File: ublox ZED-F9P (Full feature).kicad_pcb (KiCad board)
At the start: 4 copper layers, 43.2 x 43.2 mm, 143 parts, among them J1 Radio, J2 Qwiic Right Angle, J3 PTH, J4 Qwiic Right Angle, J5 USB_C_2-LAYER_PADS, J6 CONN_06NO_SILK_FEMALE_PTH, J7 CONN_09NO_SILK, U2 3.3V, U3 ZED-F9P

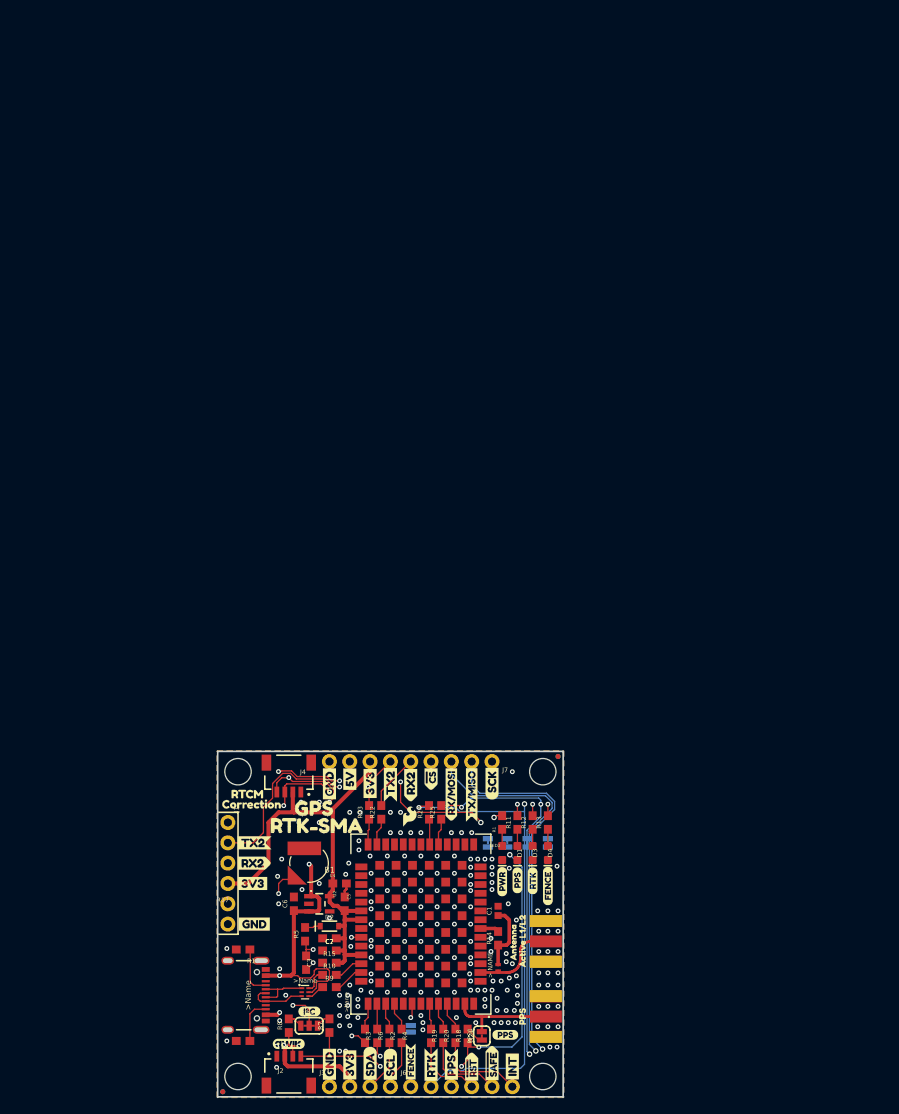
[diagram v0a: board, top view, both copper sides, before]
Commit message: removed SMA time paulse from F9H
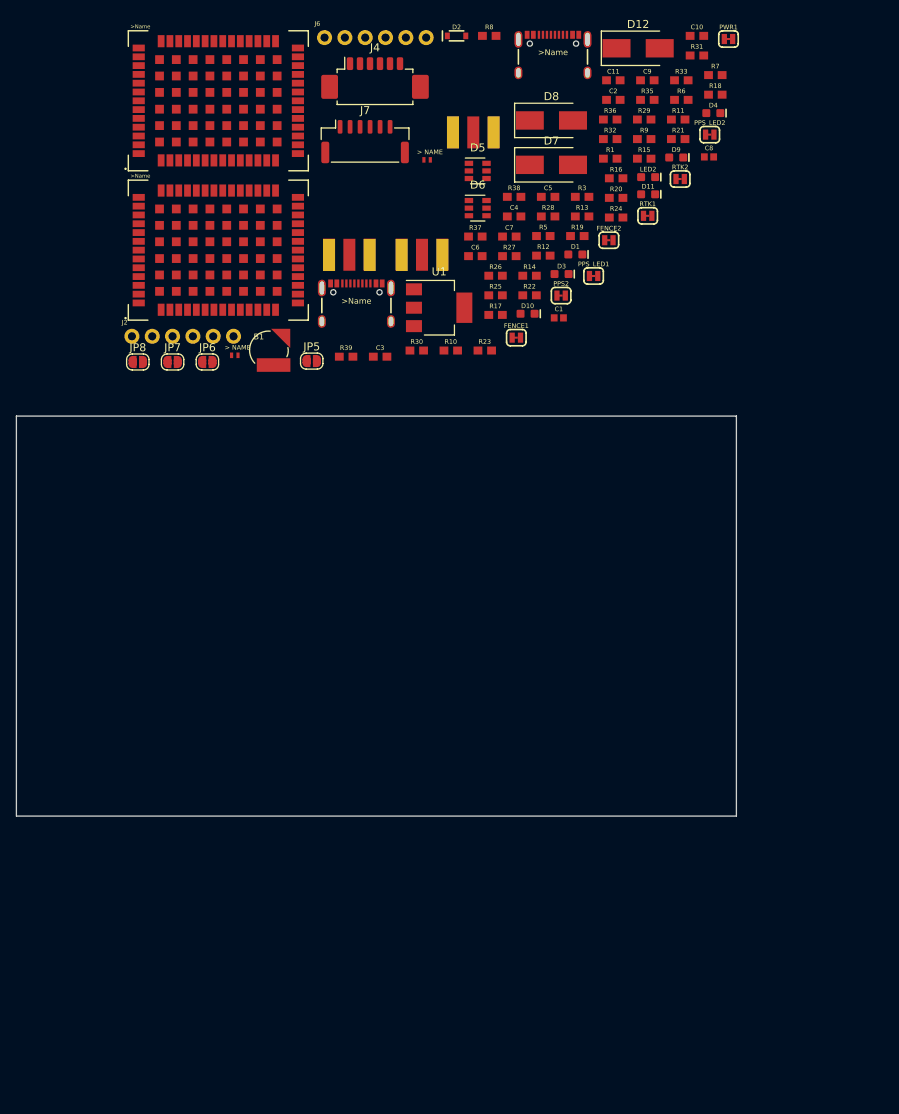
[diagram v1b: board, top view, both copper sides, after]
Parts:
- removed FRAME2: FRAME-LEDGER, Qwiic GPS-RTK-SMA - ublox ZED-F9P:CREATIVE_COMMONS
- removed J3: PTH, Qwiic GPS-RTK-SMA - ublox ZED-F9P:1X04_NO_SILK
- removed JP101, JP31, JP41, JP91: STAND-OFF, Qwiic GPS-RTK-SMA - ublox ZED-F9P:STAND-OFF
- removed JP21, JP61, JP71, JP81: FIDUCIALUFIDUCIAL, Qwiic GPS-RTK-SMA - ublox ZED-F9P:MICRO-FIDUCIAL
- removed LOGO1: OSHW-LOGOMINI, Qwiic GPS-RTK-SMA - ublox ZED-F9P:OSHW-LOGO-MINI
- removed LOGO2: SFE_LOGO_NAME_FLAME.1_INCH, Qwiic GPS-RTK-SMA - ublox ZED-F9P:SFE_LOGO_NAME_FLAME_.1
- removed PPS1: JUMPER-SMT_2_NC_TRACE_SILK, Qwiic GPS-RTK-SMA - ublox ZED-F9P:SMT-JUMPER_2_NC_TRACE_SILK
- removed R2, R4: 33, Qwiic GPS-RTK-SMA - ublox ZED-F9P:0603
- removed SPI1: JUMPER-SMT_2_NO_SILK, Qwiic GPS-RTK-SMA - ublox ZED-F9P:SMT-JUMPER_2_NO_SILK
- removed U$1, U$4: , Qwiic GPS-RTK-SMA - ublox ZED-F9P:SDA-[)
- removed U$10: , Qwiic GPS-RTK-SMA - ublox ZED-F9P:I_SUPER2_C-()-03
- removed U$11, U$54: , Qwiic GPS-RTK-SMA - ublox ZED-F9P:FENCE2
- removed U$12, U$18: , Qwiic GPS-RTK-SMA - ublox ZED-F9P:PWR-()-03
- removed U$13, U$28, U$29, U$32: , Qwiic GPS-RTK-SMA - ublox ZED-F9P:RTK1
- removed U$14, U$17: , Qwiic GPS-RTK-SMA - ublox ZED-F9P:FENCE0
- removed U$15, U$16: , Qwiic GPS-RTK-SMA - ublox ZED-F9P:INT8
- removed U$19, U$20: , Qwiic GPS-RTK-SMA - ublox ZED-F9P:5V
- removed U$2: SPECIAL_INSTRUCTIONS-ORDERING, Qwiic GPS-RTK-SMA - ublox ZED-F9P:ORDERING_INSTRUCTIONS
- removed U$21, U$56, U$58: , Qwiic GPS-RTK-SMA - ublox ZED-F9P:RX20
- removed U$22: , Qwiic GPS-RTK-SMA - ublox ZED-F9P:U#BLOX3
- removed U$23, U$24: , Qwiic GPS-RTK-SMA - ublox ZED-F9P:CS#-_]
- removed U$25, U$52, U$72: , Qwiic GPS-RTK-SMA - ublox ZED-F9P:PPS0
- removed U$26, U$31: , Qwiic GPS-RTK-SMA - ublox ZED-F9P:RX#MOSI3
- removed U$27: , Qwiic GPS-RTK-SMA - ublox ZED-F9P:DSEL0
- removed U$3, U$5: , Qwiic GPS-RTK-SMA - ublox ZED-F9P:SCL-[)
- removed U$30: , Qwiic GPS-RTK-SMA - ublox ZED-F9P:QWIIC_4MM
- removed U$33: , Qwiic GPS-RTK-SMA - ublox ZED-F9P:SFE_LOGO_FLAME_.1
- removed U$34, U$37: , Qwiic GPS-RTK-SMA - ublox ZED-F9P:TX#MISO1
- removed U$35, U$36: , Qwiic GPS-RTK-SMA - ublox ZED-F9P:#RST3
- removed U$38, U$41: , Qwiic GPS-RTK-SMA - ublox ZED-F9P:SCK-(]-04
- removed U$39, U$40: , Qwiic GPS-RTK-SMA - ublox ZED-F9P:#SAFE1
- removed U$42: , Qwiic GPS-RTK-SMA - ublox ZED-F9P:RX22
- removed U$43, U$44: , Qwiic GPS-RTK-SMA - ublox ZED-F9P:PPS5
- removed U$45, U$68: , Qwiic GPS-RTK-SMA - ublox ZED-F9P:GND3
- removed U$47, U$74: , Qwiic GPS-RTK-SMA - ublox ZED-F9P:PPS1
- removed U$48, U$70: , Qwiic GPS-RTK-SMA - ublox ZED-F9P:RTCM5
- removed U$49: , Qwiic GPS-RTK-SMA - ublox ZED-F9P:ZED#F9P6
- removed U$50, U$55, U$57: , Qwiic GPS-RTK-SMA - ublox ZED-F9P:TX21
- removed U$51: , Qwiic GPS-RTK-SMA - ublox ZED-F9P:TX23
- removed U$53, U$69: , Qwiic GPS-RTK-SMA - ublox ZED-F9P:CORRECTION0
- removed U$59: , Qwiic GPS-RTK-SMA - ublox ZED-F9P:GPS0
- removed U$6, U$60, U$61, U$66, U$67, U$7: , Qwiic GPS-RTK-SMA - ublox ZED-F9P:3V3-04
- removed U$62, U$63, U$8, U$9: , Qwiic GPS-RTK-SMA - ublox ZED-F9P:GND-04
- removed U$65: , Qwiic GPS-RTK-SMA - ublox ZED-F9P:ACTIVE_L1#L21
- removed U$71, U$75: , Qwiic GPS-RTK-SMA - ublox ZED-F9P:ANTENNA2
- removed U$73: , Qwiic GPS-RTK-SMA - ublox ZED-F9P:RTK#SMA4
- removed U$76: , Qwiic GPS-RTK-SMA - ublox ZED-F9P:GPS#RTK#SMA5
- removed U2: 3.3V, Qwiic GPS-RTK-SMA - ublox ZED-F9P:SOT23-5
- added C10: 1.0uF, Qwiic GPS-RTK-SMA - ublox ZED-F9P:0603, F.Cu at (186.8, -6.02)
- added C11: 0.1uF, Qwiic GPS-RTK-SMA - ublox ZED-F9P:0603, F.Cu at (176.4, -0.47)
- added C8: 47pF, Qwiic GPS-RTK-SMA - ublox ZED-F9P:0402, F.Cu at (188.3, 9.11)
- added C9: 1.0uF, Qwiic GPS-RTK-SMA - ublox ZED-F9P:0603, F.Cu at (180.6, -0.47)
- added D10: GREEN, Qwiic GPS-RTK-SMA - ublox ZED-F9P:LED-0603, F.Cu at (165.6, 28.7)
- added D11: BLUE, Qwiic GPS-RTK-SMA - ublox ZED-F9P:LED-0603, F.Cu at (180.7, 13.8)
- added D12: DIODE, Diode_SMD:D_SMB_Handsoldering, F.Cu at (179.5, -4.47)
- added D5: USBLC6-2SC6, Package_TO_SOT_SMD:SOT-23-6, F.Cu at (159.4, 10.9)
- added D7: D_Small_ALT, Diode_SMD:D_SMB_Handsoldering, F.Cu at (168.6, 10.1)
- added D8: D_Small_ALT, Diode_SMD:D_SMB_Handsoldering, F.Cu at (168.6, 4.55)
- added D9: Yellow, Qwiic GPS-RTK-SMA - ublox ZED-F9P:LED-0603, F.Cu at (184.2, 9.18)
- added E3: SMA, Qwiic GPS-RTK-SMA - ublox ZED-F9P:SMA-EDGE, F.Cu at (158.9, 6.04)
- added FB2: 120NH, Qwiic GPS-RTK-SMA - ublox ZED-F9P:0402_MURATA, F.Cu at (153.1, 9.47)
- added FENCE2: JUMPER-SMT_2_NC_TRACE_SILK, Qwiic GPS-RTK-SMA - ublox ZED-F9P:SMT-JUMPER_2_NC_TRACE_SILK, F.Cu at (175.8, 19.5)
- added JP6: Jumper_NO_Small, Jumper:SolderJumper-2_P1.3mm_Open_RoundedPad1.0x1.5mm, F.Cu at (125.6, 34.7)
- added JP7: Jumper_NO_Small, Jumper:SolderJumper-2_P1.3mm_Open_RoundedPad1.0x1.5mm, F.Cu at (121.3, 34.7)
- added JP8: Jumper_NO_Small, Jumper:SolderJumper-2_P1.3mm_Open_RoundedPad1.0x1.5mm, F.Cu at (116.9, 34.7)
- added PPS2: JUMPER-SMT_2_NC_TRACE_SILK, Qwiic GPS-RTK-SMA - ublox ZED-F9P:SMT-JUMPER_2_NC_TRACE_SILK, F.Cu at (169.8, 26.4)
- added PPS_LED2: JUMPER-SMT_2_NC_TRACE_SILK, Qwiic GPS-RTK-SMA - ublox ZED-F9P:SMT-JUMPER_2_NC_TRACE_SILK, F.Cu at (188.4, 6.32)
- added R26: 27, Qwiic GPS-RTK-SMA - ublox ZED-F9P:0603, F.Cu at (161.6, 24.0)
- added R27: 100k, Qwiic GPS-RTK-SMA - ublox ZED-F9P:0603, F.Cu at (163.4, 21.5)
- added R28: 33, Qwiic GPS-RTK-SMA - ublox ZED-F9P:0603, F.Cu at (168.2, 16.5)
- added R29: 33, Qwiic GPS-RTK-SMA - ublox ZED-F9P:0603, F.Cu at (180.2, 4.43)
- added R30: 33, Qwiic GPS-RTK-SMA - ublox ZED-F9P:0603, F.Cu at (151.8, 33.3)
- added R31: 33, Qwiic GPS-RTK-SMA - ublox ZED-F9P:0603, F.Cu at (186.8, -3.57)
- added R32: 33, Qwiic GPS-RTK-SMA - ublox ZED-F9P:0603, F.Cu at (176.0, 6.88)
- added R33: 33, Qwiic GPS-RTK-SMA - ublox ZED-F9P:0603, F.Cu at (184.9, -0.47)
- added R35: 1k, Qwiic GPS-RTK-SMA - ublox ZED-F9P:0603, F.Cu at (180.6, 1.98)
- added R36: 1k, Qwiic GPS-RTK-SMA - ublox ZED-F9P:0603, F.Cu at (176.0, 4.43)
- added R37: 1k, Qwiic GPS-RTK-SMA - ublox ZED-F9P:0603, F.Cu at (159.1, 19.1)
- added R38: 33, Qwiic GPS-RTK-SMA - ublox ZED-F9P:0603, F.Cu at (164.0, 14.1)
- added R39: 33, Qwiic GPS-RTK-SMA - ublox ZED-F9P:0603, F.Cu at (143.0, 34.1)
- added RTK2: JUMPER-SMT_2_NC_TRACE_SILK, Qwiic GPS-RTK-SMA - ublox ZED-F9P:SMT-JUMPER_2_NC_TRACE_SILK, F.Cu at (184.7, 11.9)
- added U1: LD1117S33TR, Package_TO_SOT_SMD:SOT-223, F.Cu at (154.6, 28.0)
- added U4: ZED-F9H, Qwiic GPS-RTK-SMA - ublox ZED-F9P:ZED-F9P, F.Cu at (127.0, 2.09)
- C4: value 1.0uF -> 10uF
- D6: value PRTR5V0U2F -> USBLC6-2SC6; footprint Qwiic GPS-RTK-SMA - ublox ZED-F9P:SOT886 -> Package_TO_SOT_SMD:SOT-23-6
- FENCE1, PPS_LED1, PWR1, RTK1: moved to F.Cu
- J1: value Radio -> USB_C_2-LAYER_PADS; footprint Qwiic GPS-RTK-SMA - ublox ZED-F9P:1X06_NO_SILK -> Qwiic GPS-RTK-SMA - ublox ZED-F9P:USB-C-16P-2LAYER-PADS
- J2: value Qwiic Right Angle -> CONN_06NO_SILK_FEMALE_PTH; footprint Qwiic GPS-RTK-SMA - ublox ZED-F9P:JST04_1MM_RA -> Qwiic GPS-RTK-SMA - ublox ZED-F9P:1X06_NO_SILK
- J4: value Qwiic Right Angle -> Molex_PicoBlade; footprint Qwiic GPS-RTK-SMA - ublox ZED-F9P:JST04_1MM_RA -> Connector_Molex:Molex_PicoBlade_53261-0671_1x06-1MP_P1.25mm_Horizontal
- J7: value CONN_09NO_SILK -> JST_GH; footprint Qwiic GPS-RTK-SMA - ublox ZED-F9P:1X09_NO_SILK -> Connector_JST:JST_GH_SM06B-GHS-TB_1x06-1MP_P1.25mm_Horizontal
- JP5: value JUMPER-SMT_3_2-NC_TRACE_SILK -> Jumper_NO_Small; footprint Qwiic GPS-RTK-SMA - ublox ZED-F9P:SMT-JUMPER_3_2-NC_TRACE_SILK -> Jumper:SolderJumper-2_P1.3mm_Open_RoundedPad1.0x1.5mm
- R3, R6: value 33 -> 5.1k
- R7: value 2.2k -> 33
- R8: value 2.2k -> 27
- moved J6 131.6 mm to (140.3, -5.81)
- moved R7 128.2 mm to (189.1, -1.12), turned to 0 degrees
- moved R8 126.2 mm to (160.9, -6.02), turned to 0 degrees
- moved J5 125.5 mm to (168.8, -6.50), turned to 0 degrees
- moved R6 123.0 mm to (184.9, 1.98), turned to 0 degrees
- moved R18 122.1 mm to (189.1, 1.33), turned to 0 degrees
- moved R16 117.5 mm to (176.7, 11.8)
- moved R21 115.1 mm to (184.5, 6.88), turned to 0 degrees
- moved R9 113.1 mm to (180.2, 6.88)
- moved D2 112.4 mm to (156.8, -6.02)
- moved C2 110.7 mm to (176.4, 1.98), turned to 0 degrees
- moved R3 108.3 mm to (172.5, 14.1), turned to 0 degrees
- moved R15 107.9 mm to (180.2, 9.33)
- moved R20 107.0 mm to (176.7, 14.2), turned to 0 degrees
- moved PWR1 104.9 mm to (190.8, -5.63), turned to 0 degrees
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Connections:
- net /D+ renamed /D+_P
- net /D- renamed /D-_P
- net /FENCE_STAT renamed /FENCE_STAT_P
- net /PPS_STAT renamed /PPS_STAT_P
- net /RTK_STAT renamed /RTK_STAT_P
- net /~RESET renamed /~RESET_P
- net /~SAFE renamed /~SAFE_P
- C4 pad 1: 3.3V -> GND
- C4 pad 2: GND -> 3.3V
- C5 pad 2: 3.3V -> Net-(C5-Pad2)
- J2 pad 1: GND -> /FENCE_STAT_H
- J2 pad 2: 3.3V -> /RTK_STAT_H
- J2 pad 3: /SDA/~CS -> /PPS_STAT_H
- J2 pad 4: /SCL/SCK -> /~RESET_H
- J4 pad 1: GND -> /Vcc
- J4 pad 2: 3.3V -> /RX_P
- J4 pad 3: /SDA/~CS -> /TX_P
- J4 pad 4: /SCL/SCK -> /RX_H
- J6 pad 6: /INT -> /INT_P
- J7 pad 1: /SCL/SCK -> /Vcc
- J7 pad 2: /TXO/MISO -> Net-(J7-Pad2)
- J7 pad 3: /RXI/MOSI -> Net-(J7-Pad3)
- J7 pad 4: /SDA/~CS -> Net-(J7-Pad4)
- J7 pad 5: /RX2 -> Net-(J7-Pad5)
- J7 pad 6: /TX2 -> GND
- JP5 pad 1: Net-(JP5-Pad1) -> Net-(J7-Pad2)
- JP5 pad 2: 3.3V -> /RX_P
- R18 pad 2: /INT -> /INT_P
- R21 pad 1: Net-(PPS1-Pad1) -> Net-(E2-PadSIG)
- R22 pad 2: /RX2 -> /RX2_P
- R23 pad 2: /TX2 -> /TX2_P
- R3 pad 1: Net-(R3-Pad1) -> GND
- R3 pad 2: /TXO/MISO -> Net-(J1-PadB5)
- R6 pad 1: Net-(R6-Pad1) -> GND
- R6 pad 2: /RXI/MOSI -> Net-(J1-PadA5)
- R7 pad 1: /SCL/SCK -> Net-(C8-Pad1)
- R7 pad 2: Net-(JP5-Pad3) -> Net-(R7-Pad2)
- R8 pad 1: /SDA/~CS -> /D+_H
- R8 pad 2: Net-(JP5-Pad1) -> Net-(R8-Pad2)
- U3 pad 42: Net-(R3-Pad1) -> Net-(R38-Pad1)
- U3 pad 43: Net-(R6-Pad1) -> Net-(R39-Pad1)
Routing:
- net 3.3V: track 124.8 -> 0.00 mm, vias 4 -> 0
- net /SCL/SCK: track 104.4 -> 0.00 mm, vias 3 -> 0
- net /SDA/~CS: track 80.0 -> 0.00 mm, vias 3 -> 0
- net /TXO/MISO: track 74.1 -> 0.00 mm, vias 2 -> 0
- net /RXI/MOSI: track 69.9 -> 0.00 mm, vias 2 -> 0
- net /FENCE_STAT_P: track 69.2 -> 0.00 mm, vias 3 -> 0
- net /RTK_STAT_P: track 66.9 -> 0.00 mm, vias 2 -> 0
- net 5V: track 53.6 -> 0.00 mm, vias 3 -> 0
- net /RX2: track 43.1 -> 0.00 mm, vias 2 -> 0
- net /PPS_STAT_P: track 38.2 -> 0.00 mm, vias 3 -> 0
- net /TX2: track 31.5 -> 0.00 mm, vias 2 -> 0
- net /BACKUP: track 20.9 -> 0.00 mm, vias 3 -> 0
- net Net-(E2-PadSIG): track 13.3 -> 0.00 mm
- net /INT: track 11.1 -> 0.00 mm
- net Net-(E1-PadSIG): track 11.1 -> 0.00 mm
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- removed copper zone on B.Cu, net GND
- removed copper zone on Bottom, net GND
- removed copper zone on F.Cu, net GND
- removed copper zone on Route2, net GND
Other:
- board size 43.2 x 43.2 mm -> 90 x 50 mm
- net class Default: clearance 0.1016 -> 0.2
- rule pad_to_mask_clearance: 0.05 -> 0
- rule trace_clearance: 0.1016 -> 0.2
- rule trace_min: 0.1524 -> 0.2
- board text removed: "4 Layer Board"
- board text removed: "Board thickness is 1.6mm"
- board text removed: "Measurements in inches"
- board text removed: "No clean process"
- board text removed: "v12-SMA"

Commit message: changed usb c
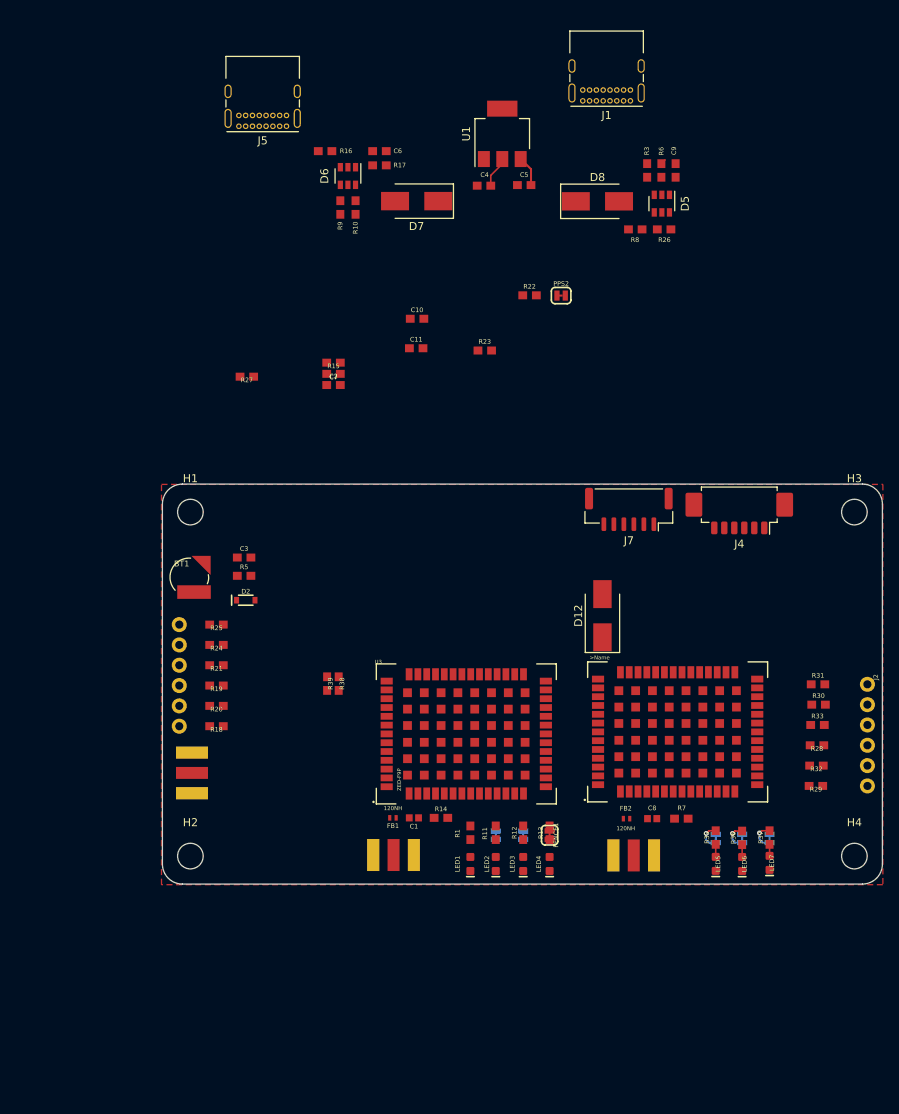
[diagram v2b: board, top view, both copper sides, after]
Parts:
- removed B1: 6.8MM_COIN_CELL, Qwiic GPS-RTK-SMA - ublox ZED-F9P:ML414H_IV01E
- removed D1, D9: Yellow, Qwiic GPS-RTK-SMA - ublox ZED-F9P:LED-0603
- removed D10, D3: GREEN, Qwiic GPS-RTK-SMA - ublox ZED-F9P:LED-0603
- removed D11, D4: BLUE, Qwiic GPS-RTK-SMA - ublox ZED-F9P:LED-0603
- removed JP5, JP6, JP7, JP8: Jumper_NO_Small, Jumper:SolderJumper-2_P1.3mm_Open_RoundedPad1.0x1.5mm
- removed PWR1: JUMPER-SMT_2_NC_TRACE_SILK, Qwiic GPS-RTK-SMA - ublox ZED-F9P:SMT-JUMPER_2_NC_TRACE_SILK
- added BT1: Battery_Cell, Qwiic GPS-RTK-SMA - ublox ZED-F9P:ML414H_IV01E, F.Cu at (123.4, 61.6)
- added H1: MountingHole, MountingHole:MountingHole_3.2mm_M3, F.Cu at (123.5, 53.5)
- added H2: MountingHole, MountingHole:MountingHole_3.2mm_M3, F.Cu at (123.5, 96.5)
- added H3: MountingHole, MountingHole:MountingHole_3.2mm_M3, F.Cu at (206.5, 53.5)
- added H4: MountingHole, MountingHole:MountingHole_3.2mm_M3, F.Cu at (206.5, 96.5)
- added LED1: RED, Qwiic GPS-RTK-SMA - ublox ZED-F9P:LED-0603, F.Cu at (158.5, 97.5)
- added LED3: GREEN, Qwiic GPS-RTK-SMA - ublox ZED-F9P:LED-0603, F.Cu at (165.1, 97.5)
- added LED4: BLUE, Qwiic GPS-RTK-SMA - ublox ZED-F9P:LED-0603, F.Cu at (168.4, 97.5)
- added LED5: Yellow, Qwiic GPS-RTK-SMA - ublox ZED-F9P:LED-0603, F.Cu at (189.2, 97.5)
- added LED6: GREEN, Qwiic GPS-RTK-SMA - ublox ZED-F9P:LED-0603, F.Cu at (192.5, 97.5)
- added LED7: BLUE, Qwiic GPS-RTK-SMA - ublox ZED-F9P:LED-0603, F.Cu at (195.9, 97.3)
- FENCE2, J6, PPS_LED1, PPS_LED2, RTK1, RTK2: moved to B.Cu
- J1, J5: footprint Qwiic GPS-RTK-SMA - ublox ZED-F9P:USB-C-16P-2LAYER-PADS -> Connector_USB:USB_C_Receptacle_GCT_USB4085
- LED2: value RED -> Yellow
- moved J2 101.7 mm to (208.1, 75.0), turned to 270 degrees
- moved R18 100.6 mm to (126.8, 80.3), turned to 180 degrees
- moved U4 97.6 mm to (184.4, 81.0)
- moved R7 93.0 mm to (184.9, 91.8)
- moved R35 92.6 mm to (189.2, 94.2), turned to 90 degrees
- moved E3 92.6 mm to (178.9, 96.4), turned to 180 degrees
- moved R11 92.0 mm to (161.7, 93.6), turned to 90 degrees
- moved R36 91.3 mm to (192.5, 94.2), turned to 90 degrees
- moved PPS_LED2 88.0 mm to (189.2, 94.3), turned to 90 degrees
- moved LED2 87.9 mm to (161.7, 97.5), turned to 270 degrees
- moved R21 87.5 mm to (126.8, 72.6), turned to 180 degrees
- moved R1 86.1 mm to (158.5, 93.6), turned to 90 degrees
- moved FB2 86.0 mm to (178.0, 91.8)
- moved R29 86.0 mm to (201.7, 87.7), turned to 180 degrees
- moved R37 83.6 mm to (195.9, 94.2), turned to 90 degrees
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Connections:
- net /Vcc renamed Net-(D12-Pad2)
- C10 pad 1: 3.3V -> +3V3
- C11 pad 2: 3.3V -> +3V3
- C2 pad 1: 3.3V -> +3V3
- C4 pad 2: 3.3V -> +3V3
- C5 pad 2: Net-(C5-Pad2) -> +5V
- C6 pad 1: 5V -> /VBUS
- C7 pad 2: 3.3V -> +3V3
- C9 pad 1: 5V -> /VBUS
- D2 pad A: 3.3V -> +3V3
- D5 pad 5: 5V -> /VBUS
- D6 pad 5: 5V -> /VBUS
- D7 pad 1: Net-(C5-Pad2) -> +5V
- D7 pad 2: 5V -> /VBUS
- D8 pad 1: Net-(C5-Pad2) -> +5V
- D8 pad 2: 5V -> /VBUS
- J2 pad 6: /INT -> /INT_H
- J4 pad 2: /RX_P -> /RX2_P
- J4 pad 3: /TX_P -> /TX2_P
- J4 pad 4: /RX_H -> /RX2_H
- J4 pad 5: /TX_H -> /TX2_H
- J7 pad 2: Net-(J7-Pad2) -> /RX2_P
- J7 pad 3: Net-(J7-Pad3) -> /TX2_P
- J7 pad 4: Net-(J7-Pad4) -> /RX2_H
- J7 pad 5: Net-(J7-Pad5) -> /TX2_H
- R1 pad 1: Net-(LED2-PadA) -> Net-(LED1-PadA)
- R1 pad 2: Net-(PWR1-Pad1) -> +3V3
- R11 pad 1: Net-(D1-PadA) -> Net-(LED2-PadA)
- R15 pad 2: 3.3V -> +3V3
- R27 pad 2: 3.3V -> +3V3
- R30 pad 2: /RTK_STAT -> /RTK_STAT_H
- U1 pad 2: 3.3V -> +3V3
- U1 pad 3: Net-(C5-Pad2) -> +5V
- U3 pad 33: 3.3V -> +3V3
- U3 pad 34: 3.3V -> +3V3
- U3 pad 38: 3.3V -> +3V3
- U4 pad 33: 3.3V -> +3V3
- U4 pad 34: 3.3V -> +3V3
- U4 pad 38: 3.3V -> +3V3
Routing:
- net Net-(PPS_LED2-Pad1): track 0.00 -> 4.29 mm, vias 0 -> 1
- net +3V3: track 0.00 -> 3.92 mm
- net +5V: track 0.00 -> 3.81 mm
- net Net-(FENCE2-Pad1): track 0.00 -> 3.61 mm, vias 0 -> 1
- net Net-(R36-Pad2): track 0.00 -> 3.47 mm, vias 0 -> 1
- net Net-(LED5-PadA): track 0.00 -> 1.56 mm
- net Net-(LED6-PadA): track 0.00 -> 1.54 mm
- net Net-(LED7-PadA): track 0.00 -> 1.44 mm
- net Net-(J1-PadA5): track 0.00 -> 0.65 mm
- added copper zone on F.Cu, net GND
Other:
- outline, holes or cut-outs redrawn
- net class Default: clearance 0.2 -> 0.2032; trace_width 0.25 -> 0.2032; via_dia 0.8 -> 0.8128; via_drill 0.4 -> 0.4064
- rule trace_clearance: 0.2 -> 0.2032
- rule trace_min: 0.2 -> 0.1524
- board text added: "PWR LED"

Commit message: changed usb c differential pair
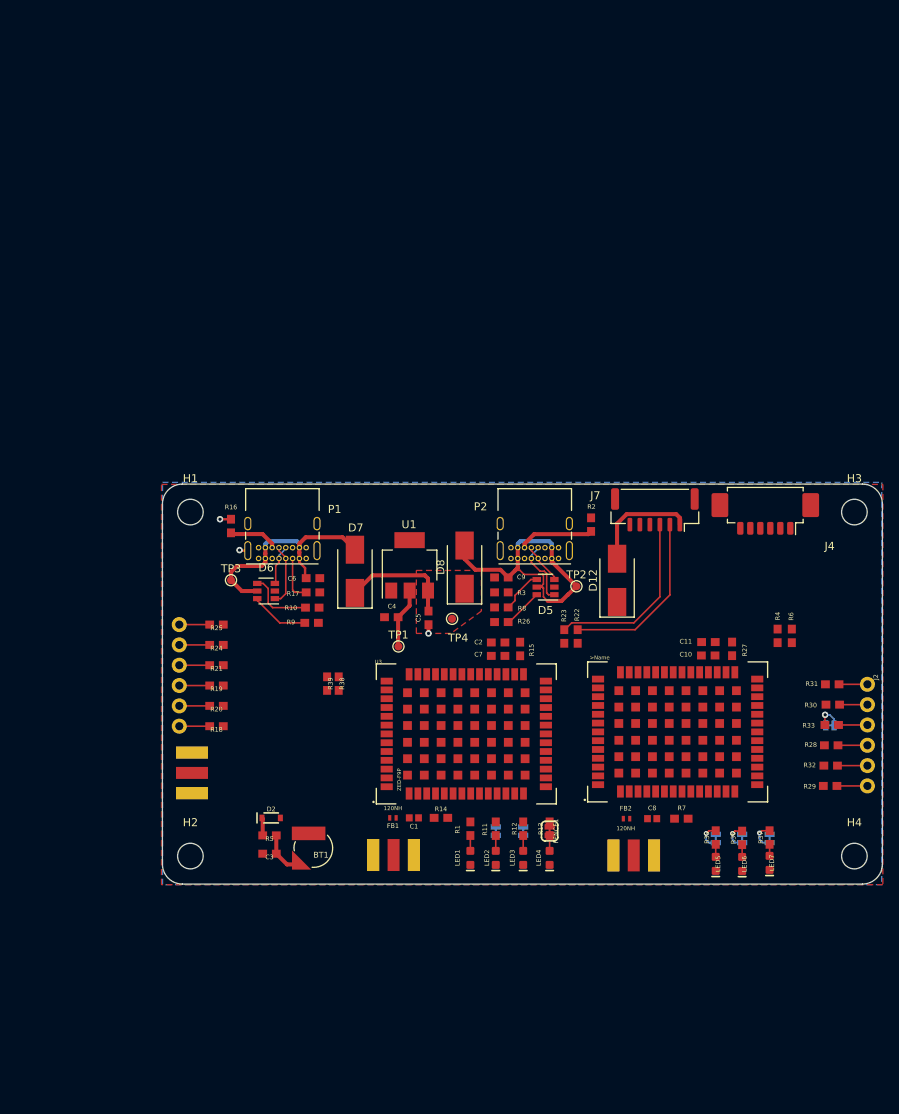
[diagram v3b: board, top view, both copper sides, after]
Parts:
- removed J1, J5: USB_C_2-LAYER_PADS, Connector_USB:USB_C_Receptacle_GCT_USB4085
- added P1: USB_C_Plug_USB2.0, Connector_USB:USB_C_Receptacle_GCT_USB4085, F.Cu at (138.0, 59.3)
- added P2: USB_C_Plug_USB2.0, Connector_USB:USB_C_Receptacle_GCT_USB4085, F.Cu at (169.5, 59.3)
- added R2: 5.1k, Qwiic GPS-RTK-SMA - ublox ZED-F9P:0603, F.Cu at (173.6, 55.1)
- added R4: 33, Qwiic GPS-RTK-SMA - ublox ZED-F9P:0603, F.Cu at (196.9, 69.0)
- added TP1: TestPoint, TestPoint:TestPoint_Pad_D1.0mm, F.Cu at (149.5, 70.3)
- added TP2: TestPoint, TestPoint:TestPoint_Pad_D1.0mm, F.Cu at (171.8, 62.8)
- added TP3: TestPoint, TestPoint:TestPoint_Pad_D1.0mm, F.Cu at (128.6, 62.0)
- added TP4: TestPoint, TestPoint:TestPoint_Pad_D1.0mm, F.Cu at (156.2, 66.8)
- PPS2: moved to B.Cu
- R6: value 5.1k -> 33
- moved R27 69.5 mm to (191.2, 70.6), turned to 90 degrees
- moved PPS2 63.4 mm to (203.4, 80.2), turned to 180 degrees
- moved R6 60.4 mm to (198.7, 69.0), turned to 270 degrees
- moved R3 55.8 mm to (162.4, 63.5), turned to 0 degrees
- moved C10 55.6 mm to (188.2, 71.4)
- moved C5 55.4 mm to (153.3, 66.7), turned to 90 degrees
- moved C9 55.3 mm to (162.4, 61.7), turned to 180 degrees
- moved U1 55.2 mm to (150.9, 60.2)
- moved C4 55.2 mm to (148.6, 66.6)
- moved C6 54.0 mm to (138.8, 61.8)
- moved R17 54.0 mm to (138.8, 63.5)
- moved R26 53.1 mm to (162.4, 67.2)
- moved D6 52.9 mm to (133.0, 63.4), turned to 180 degrees
- moved R9 52.0 mm to (138.6, 67.3), turned to 0 degrees
- moved C11 51.8 mm to (188.3, 69.7), turned to 180 degrees
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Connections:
- C6 pad 1: /VBUS -> Net-(C6-Pad1)
- C9 pad 1: /VBUS -> Net-(C9-Pad1)
- D5 pad 5: /VBUS -> Net-(C9-Pad1)
- D6 pad 4: /D+_P -> /D-_P
- D6 pad 5: /VBUS -> Net-(C6-Pad1)
- D6 pad 6: /D-_P -> /D+_P
- D7 pad 2: /VBUS -> Net-(C6-Pad1)
- D8 pad 2: /VBUS -> Net-(C9-Pad1)
- R6 pad 1: GND -> Net-(R6-Pad1)
- R6 pad 2: Net-(J1-PadA5) -> /RX2_H
- U4 pad 26: /RX2_H -> Net-(R6-Pad1)
- U4 pad 27: /TX2_H -> Net-(R4-Pad1)
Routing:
- net Net-(C9-Pad1): track 0.00 -> 37.8 mm
- net Net-(C6-Pad1): track 0.00 -> 29.7 mm
- net /TX2_P: track 0.00 -> 22.8 mm
- net /RX2_P: track 0.00 -> 22.1 mm
- net Net-(D12-Pad2): track 0.00 -> 13.8 mm
- net +5V: track 3.81 -> 14.7 mm
- net Net-(P2-PadB5): track 0.00 -> 10.2 mm
- net /D-_P: track 0.00 -> 8.35 mm
- net Net-(D5-Pad1): track 0.00 -> 8.15 mm
- net /D+_P: track 0.00 -> 7.57 mm
- net Net-(D6-Pad1): track 0.45 -> 7.71 mm
- net Net-(P1-PadB5): track 0.01 -> 6.24 mm
- net Net-(P1-PadA5): track 0.00 -> 5.76 mm
- net /BACKUP: track 0.00 -> 5.46 mm
- net /D+_H: track 0.00 -> 5.40 mm
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- added copper zone on F.Cu, net +5V
- added copper zone on B.Cu, net GND
- added copper zone on In2.Cu, net GND
